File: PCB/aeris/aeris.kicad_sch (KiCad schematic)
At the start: 47 parts, among them J1 PMSA003A, J2 SHT45, J3 LPS22HB, J4 SCD40, J5 SGP41, J6 USB-C Input, J7 OUT, Q1 BSS138, Q2 BSS138, U1 ESP32-C6-SUPERMINI, U2 74AHCT244

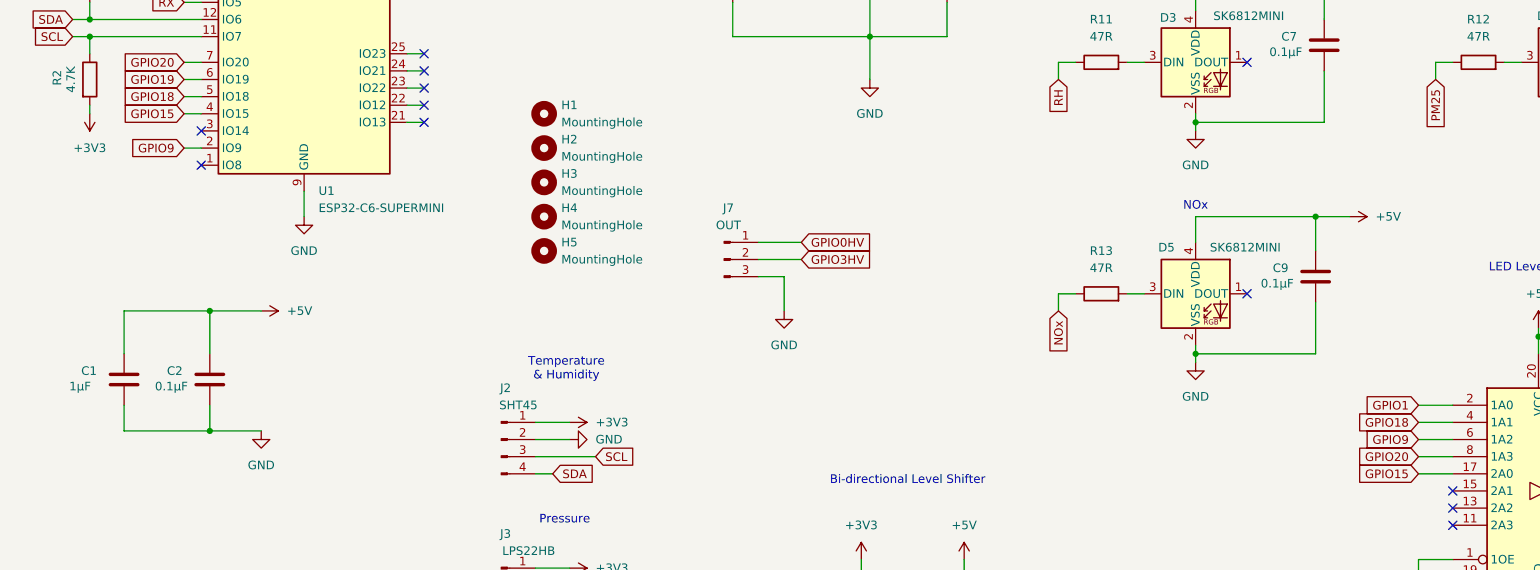
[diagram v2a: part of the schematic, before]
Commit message: Refactor PCB design and update sensor configurations
- Changed footprint references for LED components to use the correct library.
- Enhanced README with detailed sensor conversion formulas and calibration notes.
- Updated aeris_driver.c to enforce minimum sampling intervals for SGP41 and SCD40 sensors.
- Disabled automatic self-calibration for SCD40 to maintain stable CO2 baseline.
- Adjusted LPS22HB sensor configuration to use one-shot mode for power savings.
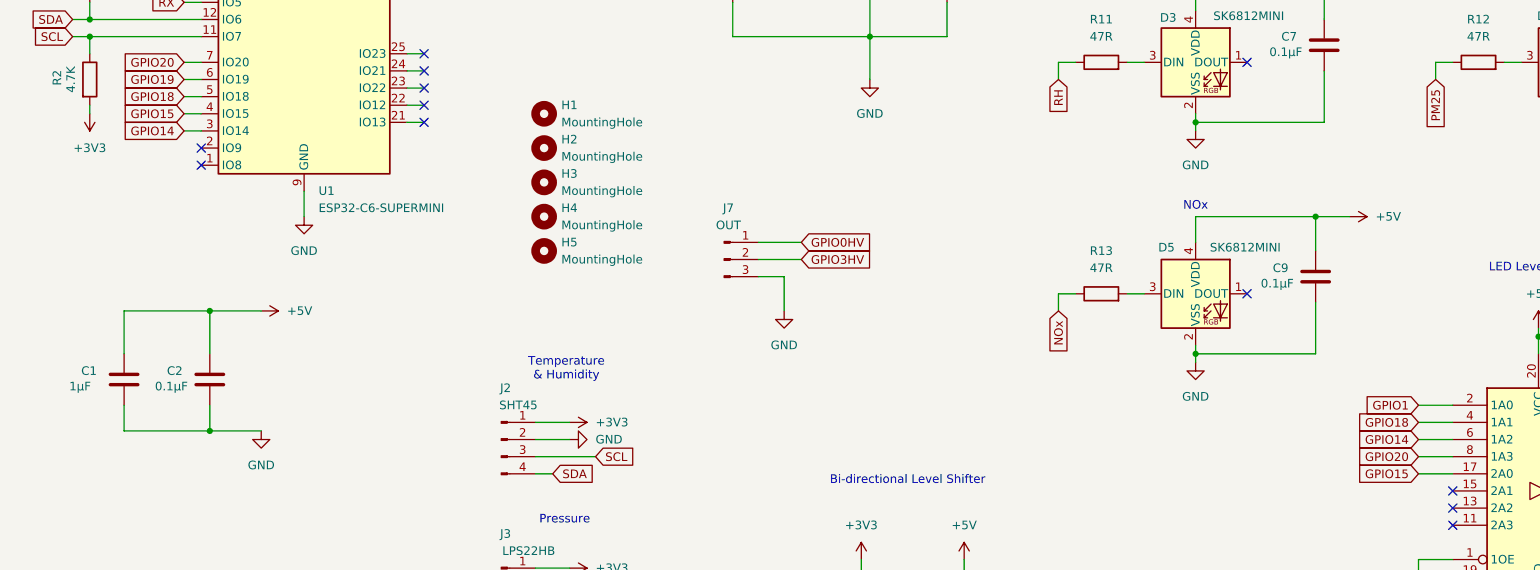
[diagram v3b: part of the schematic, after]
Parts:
- C4: footprint Capacitor_SMD:C_0805_2012Metric -> Capacitor_SMD:C_1206_3216Metric
- D1, D2, D3, D4, D5: footprint LED_SMD:LED_SK6812MINI_PLCC4_3.5x3.5mm_P1.75mm -> esp32-h2-supermini:LED_SK6812MINI_PLCC4_3.5x3.5mm_P1.75mm
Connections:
- net GPIO14: now reaches U1.3 (IO14)
- net GPIO14: now also U2.6 (1A2)
- net GPIO9: no longer names the net of U1.2 (IO9)
- net GPIO9: no longer U2.6 (1A2)
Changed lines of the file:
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@@
 	)
 	(no_connect
+		(at 39.37 77.47)
+	)
+	(no_connect
 		(at 224.79 133.35)
 	)
@@
 	)
 	(no_connect
-		(at 39.37 74.93)
-	)
-	(no_connect
 		(at 72.39 63.5)
 	)
@@
 	(wire
 		(pts
+			(xy 219.71 120.65) (xy 224.79 120.65)
+		)
+		(stroke
+			(width 0)
+			(type default)
+		)
+	)
+	(wire
+		(pts
 			(xy 26.67 166.37) (xy 43.18 166.37)
 		)
@@
 	(wire
 		(pts
-			(xy 219.71 120.65) (xy 224.79 120.65)
-		)
-		(stroke
-			(width 0)
-			(type default)
-		)
-	)
-	(wire
-		(pts
 			(xy 176.53 99.06) (xy 179.07 99.06)
 		)
@@
 	(wire
 		(pts
-			(xy 237.49 148.59) (xy 237.49 149.86)
+			(xy 36.83 74.93) (xy 39.37 74.93)
 		)
 		(stroke
@@
 	(wire
 		(pts
-			(xy 52.07 29.21) (xy 52.07 31.75)
+			(xy 237.49 148.59) (xy 237.49 149.86)
 		)
 		(stroke
@@
 	(wire
 		(pts
-			(xy 93.98 40.64) (xy 93.98 44.45)
+			(xy 52.07 29.21) (xy 52.07 31.75)
 		)
 		(stroke
@@
 	(wire
 		(pts
-			(xy 222.25 67.31) (xy 222.25 64.77)
+			(xy 93.98 40.64) (xy 93.98 44.45)
 		)
 		(stroke
@@
 	(wire
 		(pts
-			(xy 59.69 30.48) (xy 59.69 31.75)
+			(xy 222.25 67.31) (xy 222.25 64.77)
 		)
 		(stroke
@@
 	(wire
 		(pts
-			(xy 137.16 184.15) (xy 137.16 181.61)
+			(xy 59.69 30.48) (xy 59.69 31.75)
 		)
 		(stroke
@@
 	(wire
 		(pts
-			(xy 176.53 64.77) (xy 179.07 64.77)
+			(xy 137.16 184.15) (xy 137.16 181.61)
 		)
 		(stroke
@@
 	(wire
 		(pts
-			(xy 88.9 120.65) (xy 93.98 120.65)
+			(xy 176.53 64.77) (xy 179.07 64.77)
 		)
 		(stroke
@@
 	(wire
 		(pts
-			(xy 36.83 77.47) (xy 39.37 77.47)
+			(xy 88.9 120.65) (xy 93.98 120.65)
 		)
 		(stroke
@@
 		)
 	)
-	(global_label "GPIO9"
+	(global_label "GPIO14"
+		(shape input)
+		(at 36.83 74.93 180)
+		(fields_autoplaced yes)
+		(effects
+			(font
+				(size 1.27 1.27)
+			)
+			(justify right)
+		)
+		(property "Intersheetrefs" "${INTERSHEET_REFS}"
+			(at 26.9505 74.93 0)
+			(effects
+				(font
+					(size 1.27 1.27)
+				)
+				(justify right)
+				(hide yes)
+			)
+		)
+	)
+	(global_label "GPIO14"
 		(shape input)
-		(at 36.83 77.47 180)
+		(at 219.71 120.65 180)
 		(fields_autoplaced yes)
 		(effects
@@
 		)
 		(property "Intersheetrefs" "${INTERSHEET_REFS}"
-			(at 28.16 77.47 0)
+			(at 209.8305 120.65 0)
 			(effects
 				(font
@@
 		)
 	)
-	(global_label "GPIO9"
-		(shape input)
-		(at 219.71 120.65 180)
-		(fields_autoplaced yes)
-		(effects
-			(font
-				(size 1.27 1.27)
-			)
-			(justify right)
-		)
-		(property "Intersheetrefs" "${INTERSHEET_REFS}"
-			(at 211.04 120.65 0)
-			(effects
-				(font
-					(size 1.27 1.27)
-				)
-				(justify right)
-				(hide yes)
-			)
-		)
-	)
 	(global_label "CO2"
 		(shape input)
@@
 			)
 		)
-		(property "Footprint" "LED_SMD:LED_SK6812MINI_PLCC4_3.5x3.5mm_P1.75mm"
+		(property "Footprint" "esp32-h2-supermini:LED_SK6812MINI_PLCC4_3.5x3.5mm_P1.75mm"
 			(at 243.84 36.83 0)
 			(effects
@@
 			)
 		)
-		(property "Footprint" "LED_SMD:LED_SK6812MINI_PLCC4_3.5x3.5mm_P1.75mm"
+		(property "Footprint" "esp32-h2-supermini:LED_SK6812MINI_PLCC4_3.5x3.5mm_P1.75mm"
 			(at 243.84 72.39 0)
 			(effects
@@
 			)
 		)
-		(property "Footprint" "Capacitor_SMD:C_0805_2012Metric"
+		(property "Footprint" "Capacitor_SMD:C_1206_3216Metric"
 			(at 148.8948 48.26 0)
 			(effects
@@
 			)
 		)
-		(property "Footprint" "LED_SMD:LED_SK6812MINI_PLCC4_3.5x3.5mm_P1.75mm"
+		(property "Footprint" "esp32-h2-supermini:LED_SK6812MINI_PLCC4_3.5x3.5mm_P1.75mm"
 			(at 187.96 106.68 0)
 			(effects
@@
 			)
 		)
-		(property "Footprint" "LED_SMD:LED_SK6812MINI_PLCC4_3.5x3.5mm_P1.75mm"
+		(property "Footprint" "esp32-h2-supermini:LED_SK6812MINI_PLCC4_3.5x3.5mm_P1.75mm"
 			(at 187.96 72.39 0)
 			(effects
@@
 			)
 		)
-		(property "Footprint" "LED_SMD:LED_SK6812MINI_PLCC4_3.5x3.5mm_P1.75mm"
+		(property "Footprint" "esp32-h2-supermini:LED_SK6812MINI_PLCC4_3.5x3.5mm_P1.75mm"
 			(at 187.96 36.83 0)
 			(effects
